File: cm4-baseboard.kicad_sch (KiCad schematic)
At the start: 4 parts

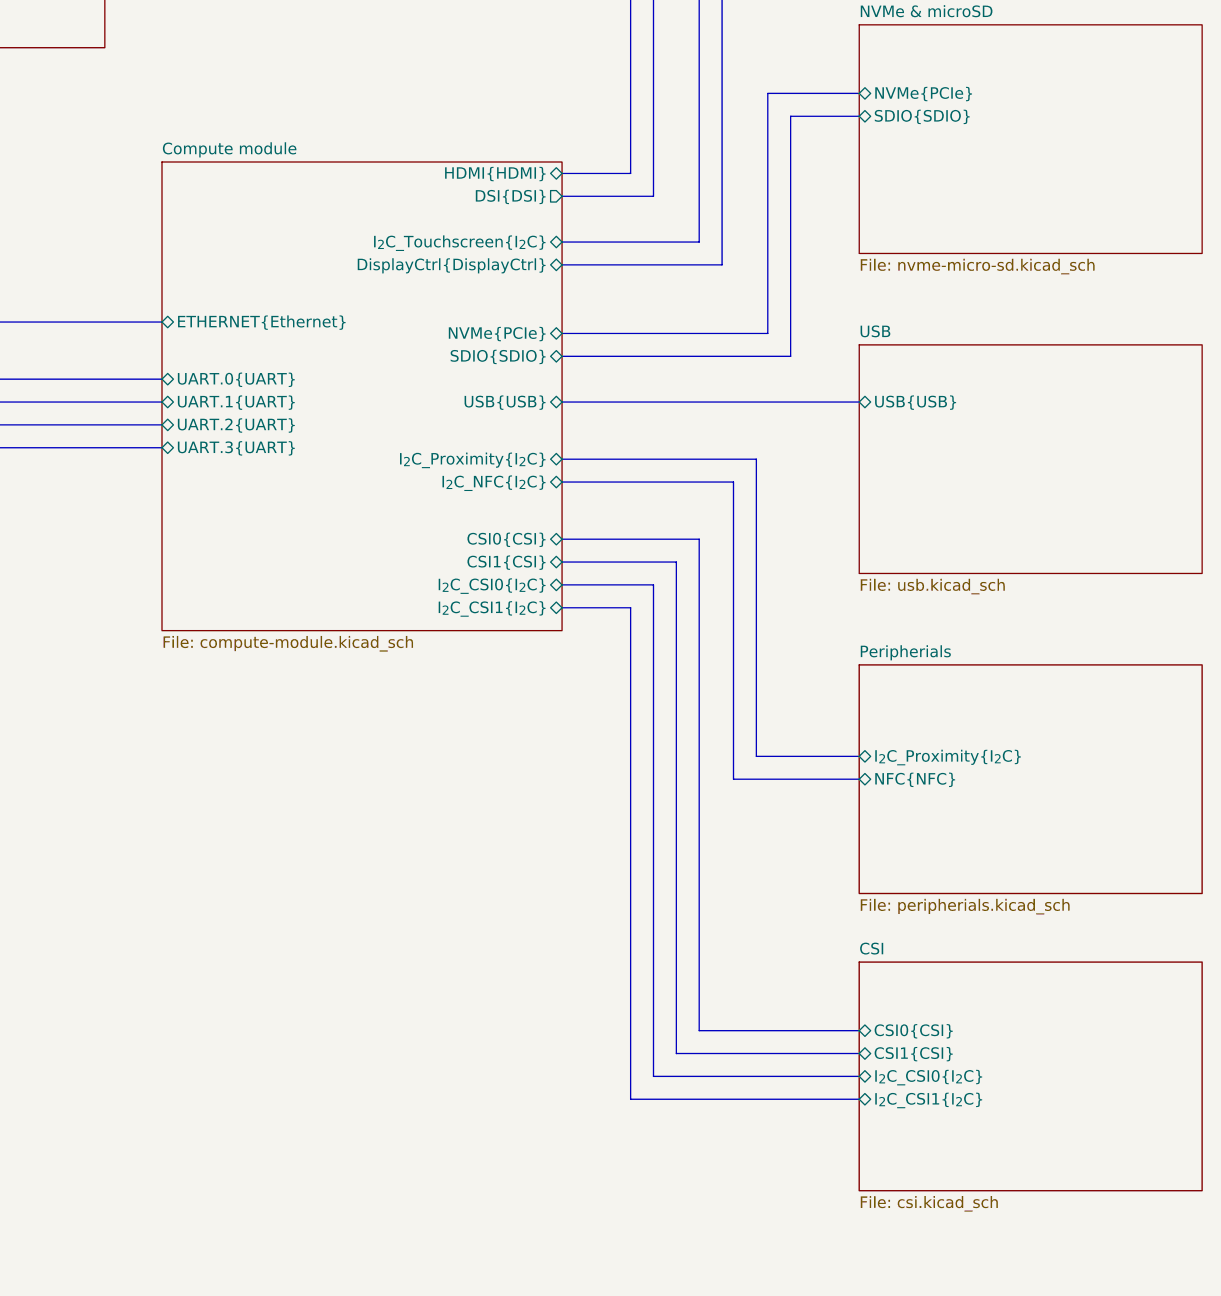
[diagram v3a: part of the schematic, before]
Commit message: [#54437] Clean CSI connections schematic
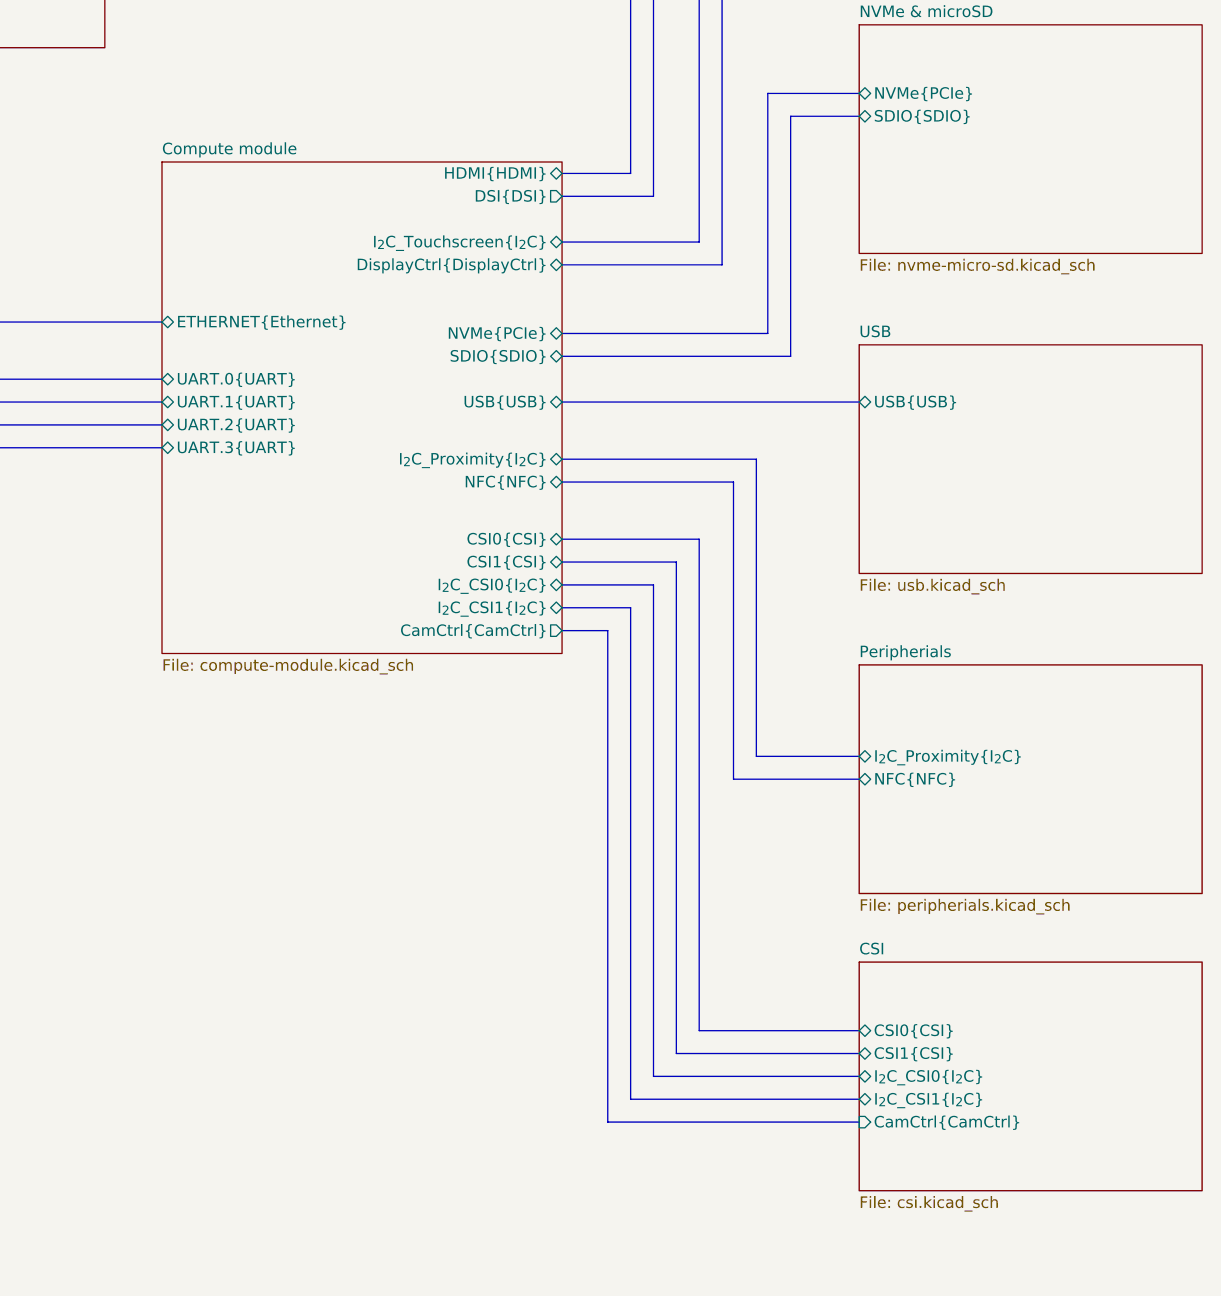
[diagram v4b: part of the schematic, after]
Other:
- sheet CSI ports: added CamCtrl{CamCtrl}; removed none
- sheet Compute module ports: added CamCtrl{CamCtrl}, NFC{NFC}; removed I_{2}C_NFC{I_{2}C}
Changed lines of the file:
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@@
   (bus_alias "I_{2}C" (members "SCL" "SDA"))
   (bus_alias "Ethernet" (members "D0_P" "D0_N" "D1_P" "D1_N" "D2_P" "D2_N" "D3_P" "D3_N" "LED_ACT" "LED_LINK"))
+  (bus_alias "USB" (members "RX_P" "RX_N" "TX_P" "TX_N" "D_P" "D_N"))
   (bus_alias "SDIO" (members "D0" "D1" "D2" "D3" "CMD" "CLK" "CD"))
   (bus_alias "PCIe" (members "TX0_P" "TX0_N" "RX0_P" "RX0_N" "CLK_P" "CLK_N" "TX1_N" "TX2_N" "TX3_N" "TX1_P" "TX2_P" "TX3_P" "RX1_N" "RX2_N" "RX3_N" "RX1_P" "RX2_P" "RX3_P" "~{RST}" "~{CLK_REQ}"))
-  (bus_alias "USB" (members "RX_P" "RX_N" "TX_P" "TX_N" "D_P" "D_N"))
   (bus_alias "CSI" (members "D0_P" "D0_N" "D1_P" "D1_N" "D2_P" "D2_N" "D3_P" "D3_N" "CLK_P" "CLK_N"))
   (junction (at 166.37 264.16) (diameter 0) (color 0 0 0 0)
@@
     (stroke (width 0) (type default) (color 0 0 0 0))
   )
+  (bus (pts (xy 248.92 208.28) (xy 276.86 208.28))
+    (stroke (width 0) (type default) (color 0 0 0 0))
+  )
   (wire (pts (xy 166.37 264.16) (xy 167.64 264.16))
     (stroke (width 0) (type default) (color 0 0 0 0))
@@
     (stroke (width 0) (type default) (color 0 0 0 0))
   )
+  (bus (pts (xy 248.92 153.67) (xy 248.92 208.28))
+    (stroke (width 0) (type default) (color 0 0 0 0))
+  )
   (bus (pts (xy 259.08 198.12) (xy 259.08 143.51))
     (stroke (width 0) (type default) (color 0 0 0 0))
@@
     (stroke (width 0) (type default) (color 0 0 0 0))
   )
+  (bus (pts (xy 243.84 153.67) (xy 248.92 153.67))
+    (stroke (width 0) (type default) (color 0 0 0 0))
+  )
   (bus (pts (xy 254 105.41) (xy 254 57.15))
     (stroke (width 0) (type default) (color 0 0 0 0))
@@
     (pin "1")
   )
-  (sheet (at 199.39 101.6) (size 44.45 52.07) (fields_autoplaced)
+  (sheet (at 199.39 101.6) (size 44.45 54.61) (fields_autoplaced)
     (stroke (width 0) (type solid) (color 0 0 0 0))
     (fill (color 0 0 0 0.0000))
@@
       (effects (font (size 1.27 1.27)) (justify left bottom))
     )
-    (property "Sheet file" "compute-module.kicad_sch" (id 1) (at 199.39 154.2546 0)
+    (property "Sheet file" "compute-module.kicad_sch" (id 1) (at 199.39 156.7946 0)
       (effects (font (size 1.27 1.27)) (justify left top))
     )
@@
       (effects (font (size 1.27 1.27)) (justify right))
     )
-    (pin "I_{2}C_NFC{I_{2}C}" bidirectional (at 243.84 137.16 0)
-      (effects (font (size 1.27 1.27)) (justify right))
-    )
     (pin "I_{2}C_Proximity{I_{2}C}" bidirectional (at 243.84 134.62 0)
       (effects (font (size 1.27 1.27)) (justify right))
@@
       (effects (font (size 1.27 1.27)) (justify right))
     )
+    (pin "NFC{NFC}" bidirectional (at 243.84 137.16 0)
+      (effects (font (size 1.27 1.27)) (justify right))
+    )
+    (pin "CamCtrl{CamCtrl}" output (at 243.84 153.67 0)
+      (effects (font (size 1.27 1.27)) (justify right))
+    )
   )
   (sheet (at 97.79 63.5) (size 38.1 25.4) (fields_autoplaced)
@@
       (effects (font (size 1.27 1.27)) (justify left))
     )
+    (pin "CamCtrl{CamCtrl}" input (at 276.86 208.28 180)
+      (effects (font (size 1.27 1.27)) (justify left))
+    )
   )
   (sheet (at 97.79 156.21) (size 38.1 25.4) (fields_autoplaced)
@@
       (reference "#PWR098") (unit 1) (value "GND") (footprint "")
     )
-    (path "/49e0afda-d892-4d16-b8c1-dc5863c48dfa/31cb3b40-b0ac-41b3-94f5-3172527574f0"
-      (reference "#PWR0100") (unit 1) (value "+3V3") (footprint "")
-    )
-    (path "/49e0afda-d892-4d16-b8c1-dc5863c48dfa/966fe872-0504-4569-83e5-c17889c3bd20"
-      (reference "#PWR0101") (unit 1) (value "+1V8") (footprint "")
-    )
-    (path "/49e0afda-d892-4d16-b8c1-dc5863c48dfa/f5413434-694e-4163-9e5d-81d6e22a3e71"
-      (reference "#PWR0102") (unit 1) (value "+3V3") (footprint "")
-    )
     (path "/49e0afda-d892-4d16-b8c1-dc5863c48dfa/e29adfe6-c160-4af4-aefd-a044b49b92b1"
       (reference "#PWR0103") (unit 1) (value "GND") (footprint "")
@@
       (reference "#PWR0107") (unit 1) (value "GND") (footprint "")
     )
-    (path "/49e0afda-d892-4d16-b8c1-dc5863c48dfa/f71a6a77-ab2c-48c2-96d3-d286c2ae4305"
-      (reference "#PWR0108") (unit 1) (value "+3V3") (footprint "")
-    )
     (path "/49e0afda-d892-4d16-b8c1-dc5863c48dfa/af4007af-1787-45f2-93a5-da017052be93"
       (reference "#PWR0109") (unit 1) (value "GND") (footprint "")
@@
       (reference "C58") (unit 1) (value "C_1u_0402") (footprint "antmicro-footprints:C_0402_1005Metric")
     )
-    (path "/49e0afda-d892-4d16-b8c1-dc5863c48dfa/cdd8ba35-4695-410f-b16c-570c020999e4"
-      (reference "C59") (unit 1) (value "C_100n_0402") (footprint "antmicro-footprints:C_0402_1005Metric")
-    )
-    (path "/49e0afda-d892-4d16-b8c1-dc5863c48dfa/683786ab-cc9e-495f-8098-00fc7c3ab48d"
-      (reference "C60") (unit 1) (value "C_100n_0402") (footprint "antmicro-footprints:C_0402_1005Metric")
-    )
     (path "/b148dc70-7270-4ae3-80a1-580624d4cd31/e2571904-3483-4c26-86aa-84acf03d06a1"
       (reference "C61") (unit 1) (value "C_100n_0402") (footprint "antmicro-footprints:C_0402_1005Metric")
@@
       (reference "R90") (unit 1) (value "R_270R_0603") (footprint "antmicro-footprints:R_0603_1608Metric")
     )
-    (path "/49e0afda-d892-4d16-b8c1-dc5863c48dfa/cc483cc4-7950-4ec1-8df3-c02936485cfd"
-      (reference "R91") (unit 1) (value "R_0R_0402") (footprint "antmicro-footprints:R_0402_1005Metric")
-    )
-    (path "/49e0afda-d892-4d16-b8c1-dc5863c48dfa/50bc9539-fde4-4d73-a364-72a3374c4d24"
-      (reference "R92") (unit 1) (value "R_0R_0402") (footprint "antmicro-footprints:R_0402_1005Metric")
-    )
-    (path "/49e0afda-d892-4d16-b8c1-dc5863c48dfa/0de92adf-1112-473b-8af5-6fe5d28ed6d4"
-      (reference "R93") (unit 1) (value "R_4x2k2_0201_array") (footprint "antmicro-footprints:R_Array_4x0201_Panasonic_EXB18V")
-    )
-    (path "/49e0afda-d892-4d16-b8c1-dc5863c48dfa/010e942c-4dc3-4f8c-ae63-e4a94708e101"
-      (reference "R94") (unit 1) (value "R_10k_0402") (footprint "antmicro-footprints:R_0402_1005Metric")
-    )
     (path "/49e0afda-d892-4d16-b8c1-dc5863c48dfa/f6d47b6c-f211-476a-9611-cd31b7498e00"
       (reference "R95") (unit 1) (value "R_100k_0402") (footprint "antmicro-footprints:R_0402_1005Metric")
@@
       (reference "R?") (unit 1) (value "R_10k_0402") (footprint "antmicro-footprints:R_0402_1005Metric")
     )
+    (path "/49e0afda-d892-4d16-b8c1-dc5863c48dfa/2f9ba1d8-2cb5-49cc-9d5f-a4528e8f66e8"
+      (reference "R?") (unit 1) (value "R_10k_0402") (footprint "antmicro-footprints:R_0402_1005Metric")
+    )
     (path "/00000000-0000-0000-0000-00005fea17c4/34cdca07-7f28-476f-8123-5a299a0345b4"
       (reference "R?") (unit 1) (value "R_0R_0402") (footprint "antmicro-footprints:R_0402_1005Metric")
@@
       (reference "U12") (unit 1) (value "AP22615A_TSOT26") (footprint "antmicro-footprints:TSOT23-6")
     )
-    (path "/49e0afda-d892-4d16-b8c1-dc5863c48dfa/19bc9dc0-0370-4532-b9a0-436f9ceae062"
-      (reference "U13") (unit 1) (value "NTS0102_XSON") (footprint "antmicro-footprints:XSON-8_1x1.95mm_P0.5mm")
-    )
     (path "/db597aea-6022-4be8-a5d9-f0f6712c4ff6/21d59530-3477-4412-bc43-dc3f867290bf"

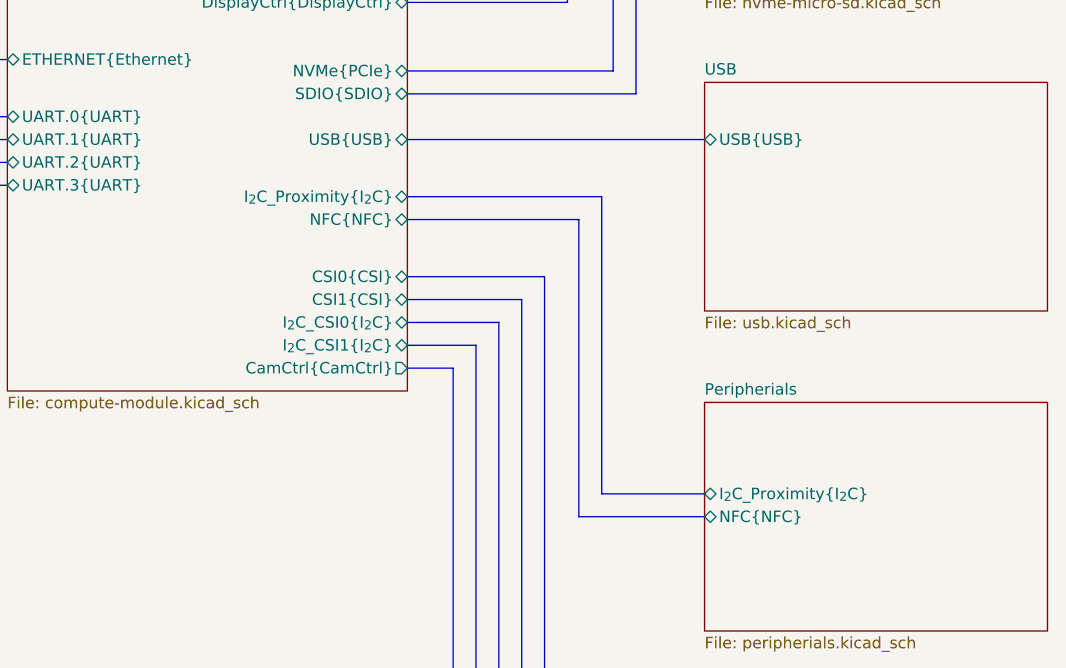
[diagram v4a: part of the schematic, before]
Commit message: [#54447] Add Sensor & LED connectors
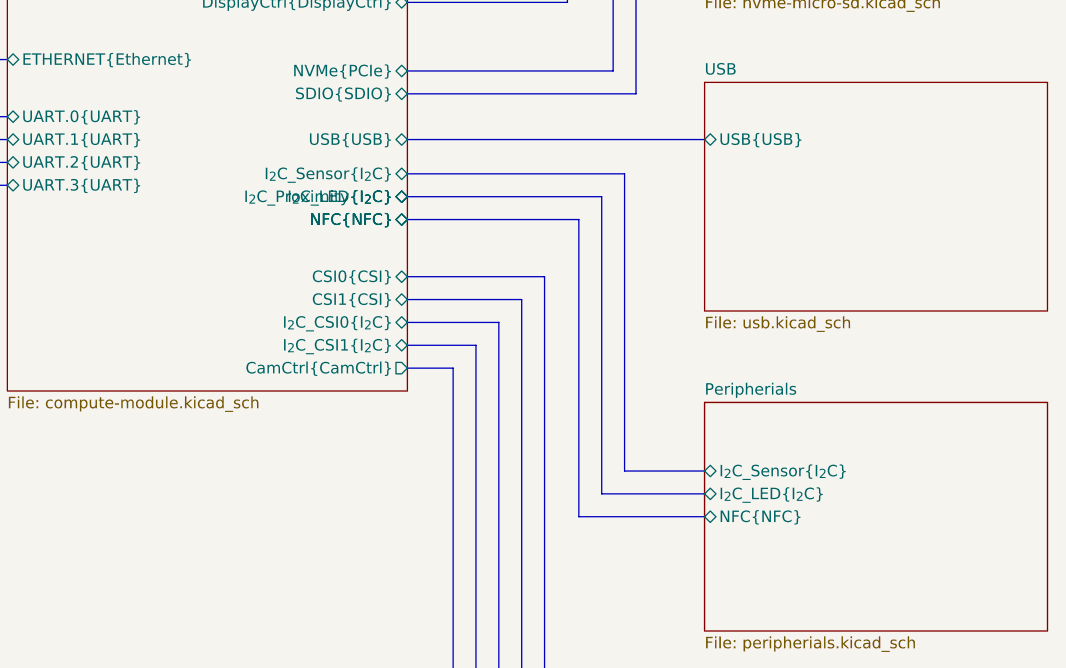
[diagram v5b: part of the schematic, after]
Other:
- sheet Compute module ports: added I_{2}C_LED{I_{2}C}, I_{2}C_Sensor{I_{2}C}; removed none
- sheet Peripherials ports: added I_{2}C_LED{I_{2}C}, I_{2}C_Sensor{I_{2}C}; removed I_{2}C_Proximity{I_{2}C}
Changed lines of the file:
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@@
     (stroke (width 0) (type default) (color 0 0 0 0))
   )
+  (bus (pts (xy 276.86 165.1) (xy 267.97 165.1))
+    (stroke (width 0) (type default) (color 0 0 0 0))
+  )
   (bus (pts (xy 276.86 167.64) (xy 265.43 167.64))
     (stroke (width 0) (type default) (color 0 0 0 0))
@@
     (stroke (width 0) (type default) (color 0 0 0 0))
   )
+  (bus (pts (xy 267.97 165.1) (xy 267.97 132.08))
+    (stroke (width 0) (type default) (color 0 0 0 0))
+  )
   (bus (pts (xy 276.86 198.12) (xy 259.08 198.12))
     (stroke (width 0) (type default) (color 0 0 0 0))
@@
     (stroke (width 0) (type default) (color 0 0 0 0))
   )
+  (bus (pts (xy 267.97 132.08) (xy 243.84 132.08))
+    (stroke (width 0) (type default) (color 0 0 0 0))
+  )
   (bus (pts (xy 276.86 54.61) (xy 251.46 54.61))
     (stroke (width 0) (type default) (color 0 0 0 0))
@@
       (effects (font (size 1.27 1.27)) (justify right))
     )
+    (pin "NFC{NFC}" bidirectional (at 243.84 137.16 0)
+      (effects (font (size 1.27 1.27)) (justify right))
+    )
+    (pin "I_{2}C_Sensor{I_{2}C}" bidirectional (at 243.84 132.08 0)
+      (effects (font (size 1.27 1.27)) (justify right))
+    )
+    (pin "I_{2}C_LED{I_{2}C}" bidirectional (at 243.84 134.62 0)
+      (effects (font (size 1.27 1.27)) (justify right))
+    )
   )
   (sheet (at 97.79 63.5) (size 38.1 25.4) (fields_autoplaced)
@@
       (effects (font (size 1.27 1.27)) (justify left top))
     )
-    (pin "I_{2}C_Proximity{I_{2}C}" bidirectional (at 276.86 167.64 180)
+    (pin "NFC{NFC}" bidirectional (at 276.86 170.18 180)
+      (effects (font (size 1.27 1.27)) (justify left))
+    )
+    (pin "I_{2}C_LED{I_{2}C}" bidirectional (at 276.86 167.64 180)
       (effects (font (size 1.27 1.27)) (justify left))
     )
-    (pin "NFC{NFC}" bidirectional (at 276.86 170.18 180)
+    (pin "I_{2}C_Sensor{I_{2}C}" bidirectional (at 276.86 165.1 180)
       (effects (font (size 1.27 1.27)) (justify left))
     )
@@
       (reference "#PWR0140") (unit 1) (value "GND") (footprint "")
     )
-    (path "/db597aea-6022-4be8-a5d9-f0f6712c4ff6/a18fdb0d-e880-425d-b8f8-6834b845e3ab"
-      (reference "#PWR0141") (unit 1) (value "+3V3") (footprint "")
-    )
-    (path "/db597aea-6022-4be8-a5d9-f0f6712c4ff6/8d34cbc0-68b5-46e1-8119-ca950a2ecfc5"
-      (reference "#PWR0142") (unit 1) (value "GND") (footprint "")
-    )
     (path "/db597aea-6022-4be8-a5d9-f0f6712c4ff6/30d606e4-a659-49e3-af30-4a900f6b5a44"
       (reference "#PWR0143") (unit 1) (value "GND") (footprint "")
@@
       (reference "J16") (unit 1) (value "USB-C_GCT_USB4105-GF-A") (footprint "antmicro-footprints:USB-C_Receptacle_GCT_USB4105-GF-A")
     )
+    (path "/db597aea-6022-4be8-a5d9-f0f6712c4ff6/171ac67e-1b08-40d3-afb0-bd926d38e2d0"
+      (reference "J?") (unit 1) (value "JST_SH_1x4_SM04B-SRSS-TB-LF-SN") (footprint "antmicro-footprints:Conn_JST_SH_1x4_SM04B-SRSS-TB-LF-SN")
+    )
     (path "/db597aea-6022-4be8-a5d9-f0f6712c4ff6/5202eabf-7a64-44f5-99ad-8ff513822683"
       (reference "J?") (unit 1) (value "U_FL-R-SMT-1") (footprint "antmicro-footprints:Coax_Conn_U.FL")
@@
       (reference "R?") (unit 1) (value "R_0R_0402") (footprint "antmicro-footprints:R_0402_1005Metric")
     )
+    (path "/db597aea-6022-4be8-a5d9-f0f6712c4ff6/ca0f824e-8b6f-487f-9025-30e791ce7609"
+      (reference "R?") (unit 1) (value "R_0R_0402") (footprint "antmicro-footprints:R_0402_1005Metric")
+    )

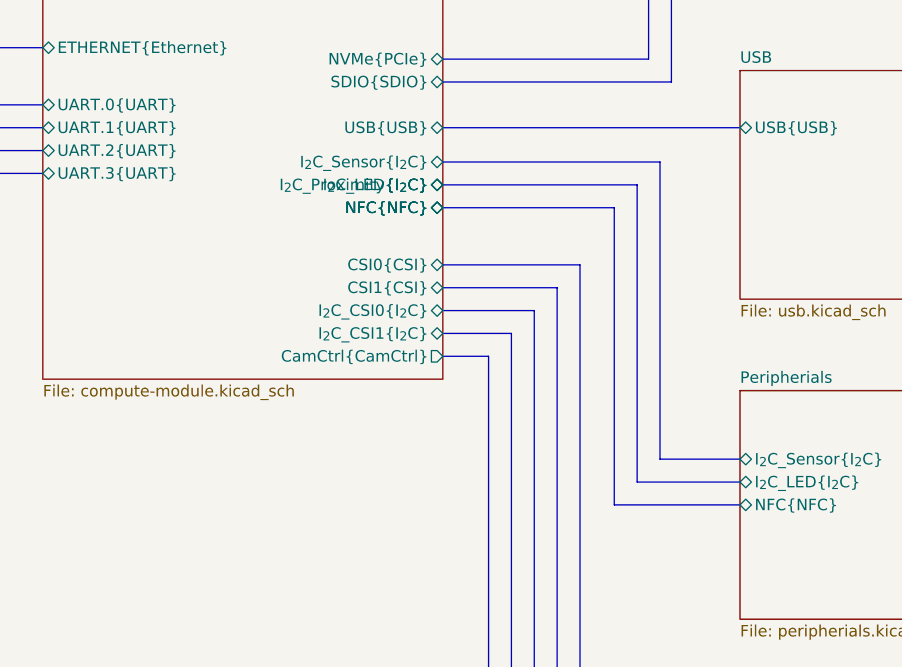
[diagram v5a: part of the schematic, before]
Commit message: [#54447] Start CM4 connections
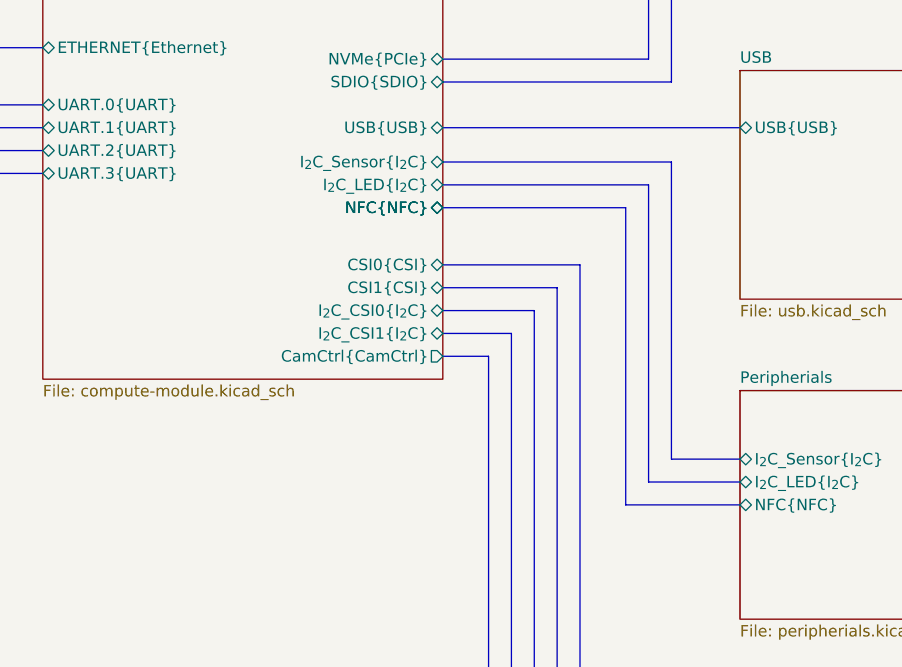
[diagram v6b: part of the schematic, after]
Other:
- sheet Compute module ports: added none; removed I_{2}C_Proximity{I_{2}C}
